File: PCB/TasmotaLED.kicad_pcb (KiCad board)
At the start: 2 copper layers, 38 x 17 mm, 15 parts, among them J1 PWR_IN, J2 ESP-01S, J3 LED_OUT, Q1 KIA30N06B, SW1 SW_Push, U1 AMS1117-3.3

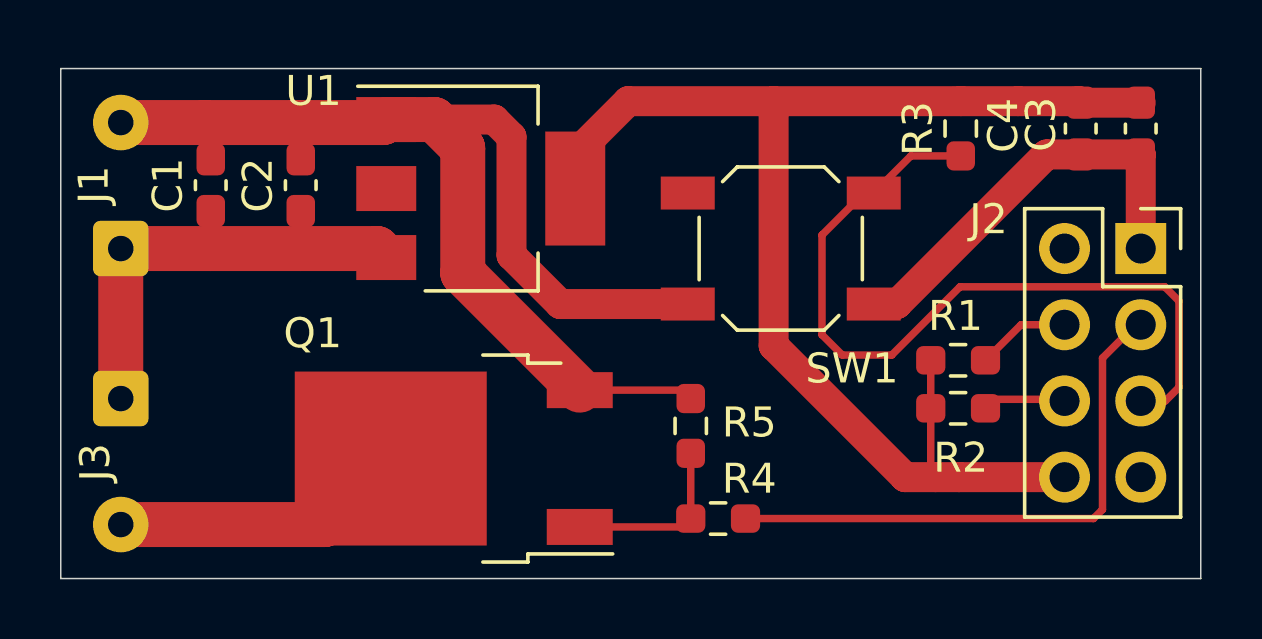
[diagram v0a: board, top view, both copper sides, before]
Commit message: Flipped ESP01S module 180 degrees to make module smaller and wiring simpler. Button is now below module and might need to be replaced with a side-actuated one.
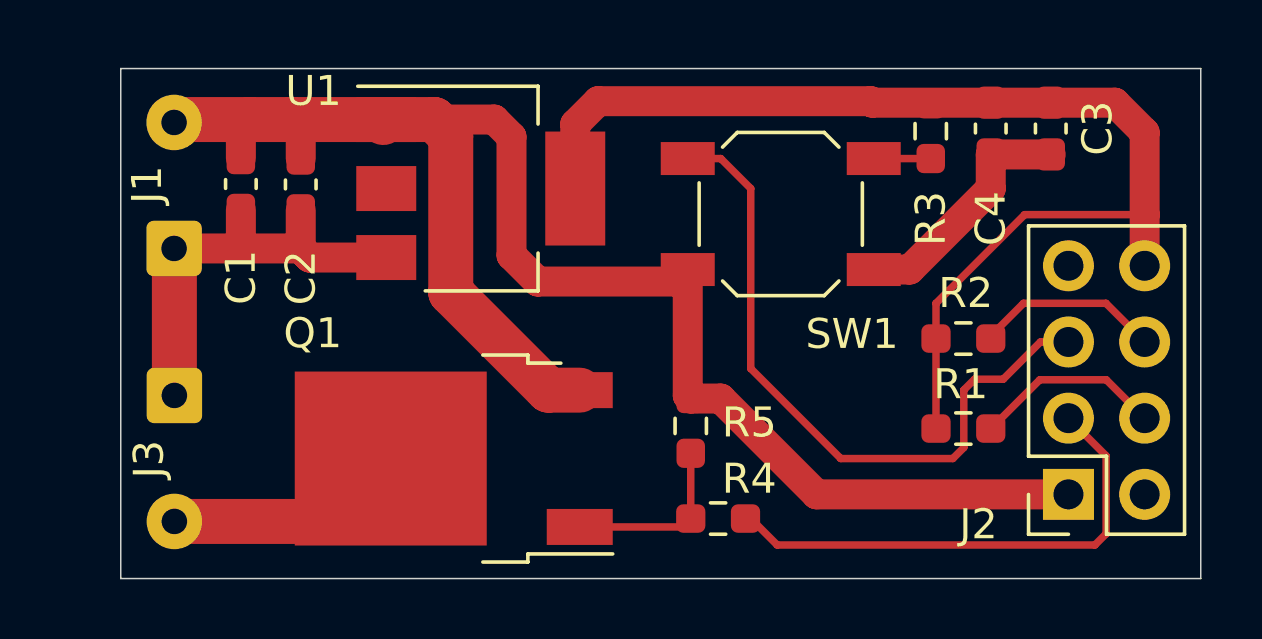
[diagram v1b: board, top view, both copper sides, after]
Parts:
- moved J2 8.54 mm to (165.6, 92.2), turned to 180 degrees
- moved C3 3.00 mm to (165.0, 80.0)
- moved C4 3.00 mm to (163.0, 80.0)
- moved R2 2.33 mm to (162.1, 87.0)
- moved R1 2.28 mm to (162.1, 90.0)
- moved J3 1.79 mm to (135.8, 88.9)
- moved J1 1.78 mm to (135.8, 84.0)
- moved SW1 1.15 mm to (156.0, 82.8)
- moved C1 1.00 mm to (138.0, 81.8)
- moved R3 1.00 mm to (161.0, 80.1)
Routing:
- net GND: track 55.5 -> 63.3 mm
- net +3V3: track 44.7 -> 39.8 mm
- net Net-(J2-Pad6): track 2.75 -> 6.20 mm
- net Net-(J2-Pad4): track 3.13 -> 6.33 mm
- net /LED_ON: track 19.3 -> 16.9 mm
- net Net-(J3-Pad2): track 9.91 -> 8.08 mm
- net /~BTN: track 26.7 -> 25.1 mm
- net +12V: track 16.5 -> 15.1 mm
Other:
- board size 38 x 17 mm -> 36 x 17 mm
